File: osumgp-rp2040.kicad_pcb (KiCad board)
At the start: 2 copper layers, 130 x 51 mm, 92 parts, among them J1 USB_C_Receptacle_USB2.0, J2 SWD, J3 USB, J4 I2C, SW1 BOOTSEL, SW2 RST, SW3 Alpsalpine_RKJXV, SW4 Alpsalpine_RKJXV, U2 W25Q16JVUXIQ, U4 USBLC6-2P6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

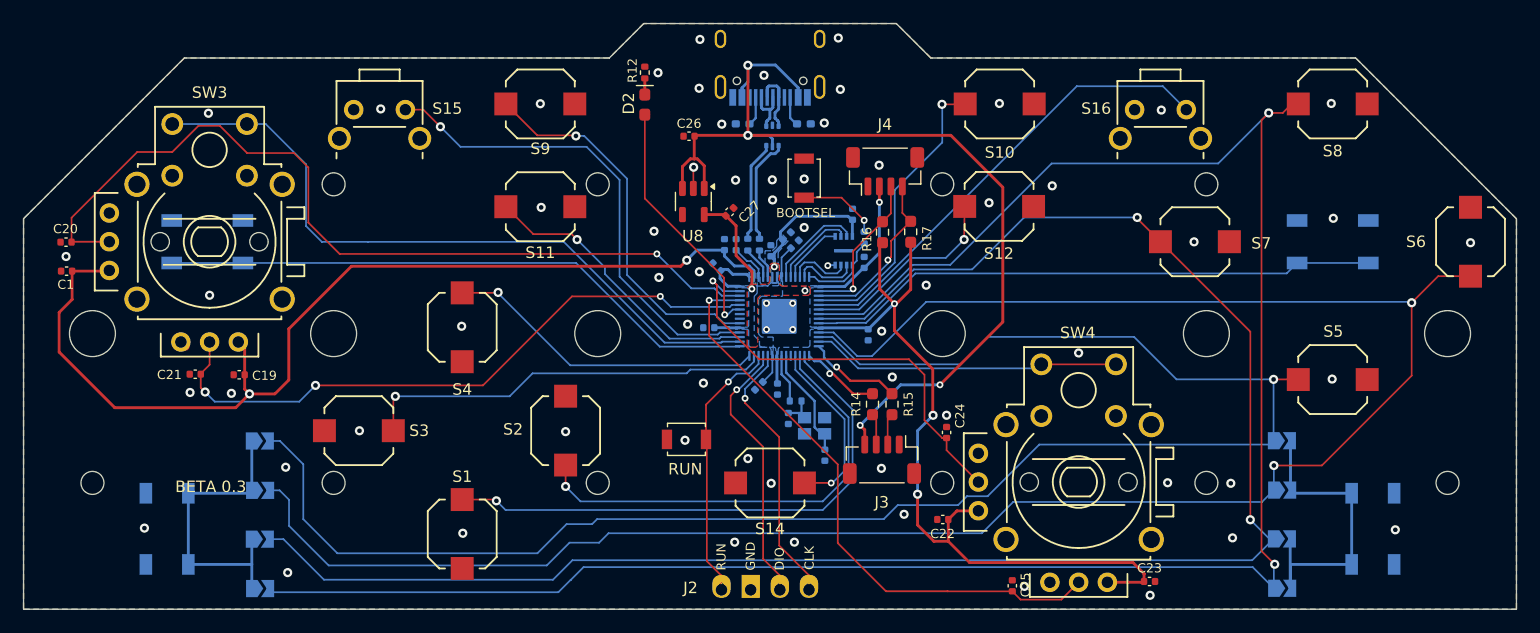
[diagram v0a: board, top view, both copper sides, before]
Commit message: Adust trace widths, component placement, and routing to pass DRC
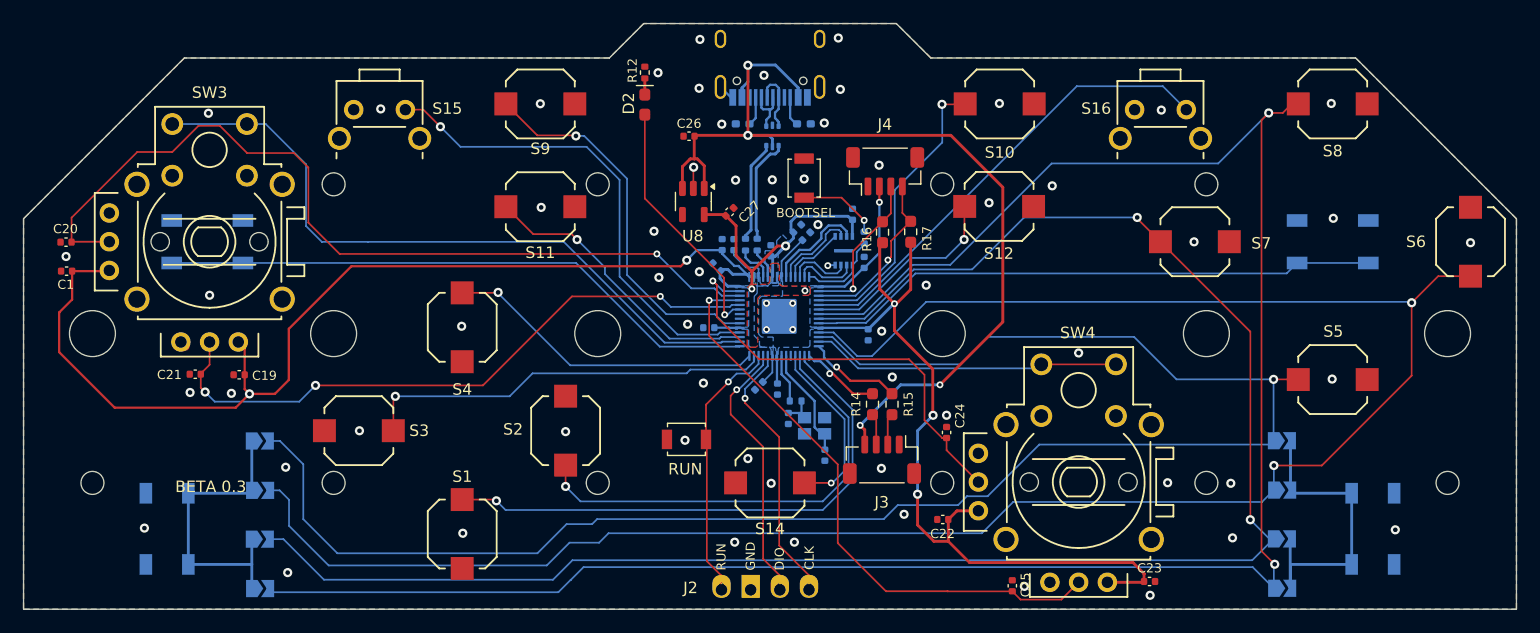
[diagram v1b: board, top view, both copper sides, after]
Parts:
- moved C8 1.22 mm to (120.5, 57.3)
- moved C15 1.12 mm to (119.8, 56.6)
- moved C10 0.20 mm to (114.2, 58.0)
- moved C12 0.20 mm to (113.2, 58.0)
- moved R8 0.20 mm to (116.3, 58.0)
- moved R9 0.20 mm to (115.2, 58.0)
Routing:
- net +3V3: track 204.3 -> 207.7 mm
- net +1V1: track 8.78 -> 10.4 mm
- net GND: track 4.05 -> 5.50 mm
